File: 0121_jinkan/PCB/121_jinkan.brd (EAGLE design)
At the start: 25.4 x 33 mm, 12 parts

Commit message: 121_jinkan　ロゴ修正、リファイン
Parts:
- removed U$3: (no value), FaBo-etc:LOGO_FABO_MS_BOTTOM
- added LOGO1: (no value), component:LOGO_FABO_M
- turned R3 to 180 degrees
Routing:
- net GND: track 88.1 -> 0.00 mm, vias 14 -> 24
- net VCC: track 38.8 -> 33.4 mm
- net I/O: track 9.37 -> 11.2 mm
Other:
- board text added: "Rev.1.0.2"
- board text removed: "Rev.1.0.1"

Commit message: #121  jinkan 分圧出力回路追加
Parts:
- added R4: 9.1K, FaBo-Resistors:0603
- added SJ1: (no value), jumper:SJW
- R3: value 5.6K -> 4.7K
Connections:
- new net N$3: R4.2, SJ1.1
- net GND: now also R4.1
- net I/O: now also SJ1.2
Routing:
- net GND: track 0.00 -> 15.1 mm, vias 24 -> 23
- net I/O: track 11.2 -> 17.4 mm
- net N$3: track 0.00 -> 2.98 mm
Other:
- board text added: "Rev.1.0.3"
- board text removed: "Rev.1.0.2"
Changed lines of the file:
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@@
 <?xml version="1.0" encoding="utf-8"?>
 <!DOCTYPE eagle SYSTEM "eagle.dtd">
-<eagle version="9.6.2">
+<eagle version="9.6.0">
 <drawing>
 <settings>
-<setting alwaysvectorfont="no"/>
+<setting alwaysvectorfont="yes"/>
 <setting keepoldvectorfont="yes"/>
 <setting verticaltext="up"/>
@@
 <plain>
 <text x="3.81" y="12.065" size="1.27" layer="21" font="vector" ratio="15" rot="R90" align="bottom-center">Jinkan</text>
-<text x="5.08" y="8.89" size="1.016" layer="21" font="vector" ratio="15" rot="R90">Rev.1.0.2</text>
+<text x="5.08" y="8.89" size="1.016" layer="21" font="vector" ratio="15" rot="R90">Rev.1.0.3</text>
 <text x="22.86" y="12.065" size="0.762" layer="21" font="vector" ratio="15" rot="R90" align="top-center">Designed in Aizu</text>
 <text x="12.7" y="13.335" size="2.54" layer="21" font="vector" ratio="15" align="bottom-center">#121</text>
 <rectangle x1="13.5" y1="9.9" x2="18.7" y2="17.5" layer="22" rot="R90"/>
 <text x="7.885" y="13.45" size="2.5" layer="22" font="vector" ratio="15" rot="MR180">M</text>
+<rectangle x1="2.54" y1="13.335" x2="6.35" y2="14.605" layer="42"/>
+<rectangle x1="2.54" y1="14.605" x2="3.175" y2="15.875" layer="42"/>
+<rectangle x1="5.715" y1="14.605" x2="6.35" y2="15.875" layer="42"/>
+<rectangle x1="2.54" y1="12.065" x2="3.175" y2="13.335" layer="42"/>
+<rectangle x1="5.715" y1="12.065" x2="6.35" y2="13.335" layer="42"/>
 </plain>
 <attributes>
@@
 </element>
 <element name="U$5" library="FaBo-Transistor" package="SOT-23" value="TRANSISTOR-NPN" x="10.6" y="18.7" smashed="yes" rot="MR180"/>
-<element name="R3" library="FaBo-Resistors" package="0603" value="5.6K" x="9.7" y="15.9" smashed="yes" rot="MR180">
+<element name="R3" library="FaBo-Resistors" package="0603" value="4.7K" x="9.7" y="15.9" smashed="yes" rot="MR180">
 <attribute name="VALUE" x="9.9" y="16" size="0.8128" layer="28" font="vector" ratio="12" rot="MR180" align="center"/>
 </element>
@@
 <element name="U$7" library="FaBo-etc" package="MARK_POINT_3MM" value="" x="19.9" y="26.7" smashed="yes" rot="MR0"/>
 <element name="LOGO1" library="component" package="LOGO_FABO_M" value="" x="22.86" y="12.065" smashed="yes" rot="R90"/>
+<element name="R4" library="FaBo-Resistors" package="0603" value="9.1K" x="6.35" y="10.16" smashed="yes" rot="MR90">
+<attribute name="VALUE" x="6.35" y="10.16" size="0.8128" layer="28" font="vector" ratio="12" rot="MR90" align="center"/>
+</element>
+<element name="SJ1" library="jumper" library_urn="urn:adsk.eagle:library:252" package="SJW" package3d_urn="urn:adsk.eagle:package:15507/1" value="" x="4.445" y="13.97" smashed="yes" rot="MR90">
+<attribute name="NAME" x="6.223" y="11.811" size="1.27" layer="26" font="vector" ratio="15" rot="MR90"/>
+<attribute name="POPULARITY" value="3" x="0.635" y="14.605" size="1.778" layer="28" rot="MR90" display="off"/>
+<attribute name="VALUE" x="4.445" y="14.97" size="0.02" layer="28" rot="MR90"/>
+</element>
 </elements>
 <signals>
@@
 <via x="10.16" y="14.351" extent="1-16" drill="0.3048"/>
 <via x="13.97" y="12.319" extent="1-16" drill="0.3048"/>
-<via x="7.493" y="12.192" extent="1-16" drill="0.3048"/>
+<via x="8.128" y="9.017" extent="1-16" drill="0.3048"/>
 <via x="7.112" y="15.494" extent="1-16" drill="0.3048"/>
 <via x="7.366" y="18.415" extent="1-16" drill="0.3048"/>
@@
 <via x="8.128" y="24.384" extent="1-16" drill="0.3048"/>
 <via x="6.858" y="21.971" extent="1-16" drill="0.3048"/>
-<via x="7.493" y="10.287" extent="1-16" drill="0.3048"/>
-<via x="7.493" y="8.382" extent="1-16" drill="0.3048"/>
+<via x="7.493" y="7.747" extent="1-16" drill="0.3048"/>
+<contactref element="R4" pad="1"/>
+<wire x1="6.35" y1="6.35" x2="8.255" y2="4.445" width="0.4064" layer="16"/>
+<wire x1="14.7" y1="5.81" x2="14.7" y2="8.255" width="0.4064" layer="16"/>
+<wire x1="6.35" y1="9.31" x2="6.35" y2="6.35" width="0.4064" layer="16"/>
+<wire x1="8.255" y1="4.445" x2="13.335" y2="4.445" width="0.4064" layer="16"/>
+<wire x1="13.335" y1="4.445" x2="14.7" y2="5.81" width="0.4064" layer="16"/>
 </signal>
 <signal name="I/O">
@@
 <wire x1="9.88" y1="17.5" x2="10.6" y2="17.5" width="0.4064" layer="16"/>
 <wire x1="8.85" y1="15.9" x2="8.85" y2="16.47" width="0.4064" layer="16"/>
-<wire x1="8.85" y1="16.47" x2="9.88" y2="17.5" width="0.4064" layer="16"/>
+<wire x1="8.85" y1="16.47" x2="9.525" y2="17.145" width="0.4064" layer="16"/>
+<wire x1="9.525" y1="17.145" x2="9.88" y2="17.5" width="0.4064" layer="16"/>
 <wire x1="10.7" y1="10.89" x2="10.7" y2="8.255" width="0.4064" layer="16"/>
 <wire x1="8.85" y1="15.9" x2="8.85" y2="12.74" width="0.4064" layer="16"/>
 <wire x1="8.85" y1="12.74" x2="10.7" y2="10.89" width="0.4064" layer="16"/>
+<contactref element="SJ1" pad="2"/>
+<wire x1="4.445" y1="15.24" x2="4.445" y2="15.875" width="0.4064" layer="16"/>
+<wire x1="4.445" y1="15.875" x2="5.715" y2="17.145" width="0.4064" layer="16"/>
+<wire x1="5.715" y1="17.145" x2="9.525" y2="17.145" width="0.4064" layer="16"/>
 </signal>
 <signal name="VCC">
@@
 <wire x1="9.65" y1="20.4" x2="9.65" y2="19.9" width="0.4064" layer="16"/>
 </signal>
+<signal name="N$3">
+<contactref element="R4" pad="2"/>
+<contactref element="SJ1" pad="1"/>
+<wire x1="4.445" y1="12.7" x2="5.08" y2="12.065" width="0.4064" layer="16"/>
+<wire x1="5.08" y1="12.065" x2="5.08" y2="11.43" width="0.4064" layer="16"/>
+<wire x1="5.08" y1="11.43" x2="5.5" y2="11.01" width="0.4064" layer="16"/>
+<wire x1="5.5" y1="11.01" x2="6.35" y2="11.01" width="0.4064" layer="16"/>
+</signal>
 </signals>
 <mfgpreviewcolors>
@@
 </board>
 </drawing>
+<compatibility>
+<note version="8.2" severity="warning">
+Since Version 8.2, EAGLE supports online libraries. The ids
+of those online libraries will not be understood (or retained)
+with this version.
+</note>
+<note version="8.3" severity="warning">
+Since Version 8.3, EAGLE supports URNs for individual library
+assets (packages, symbols, and devices). The URNs of those assets
+will not be understood (or retained) with this version.
+</note>
+<note version="8.3" severity="warning">
+Since Version 8.3, EAGLE supports the association of 3D packages
+with devices in libraries, schematics, and board files. Those 3D
+packages will not be understood (or retained) with this version.
+</note>
+</compatibility>
 </eagle>

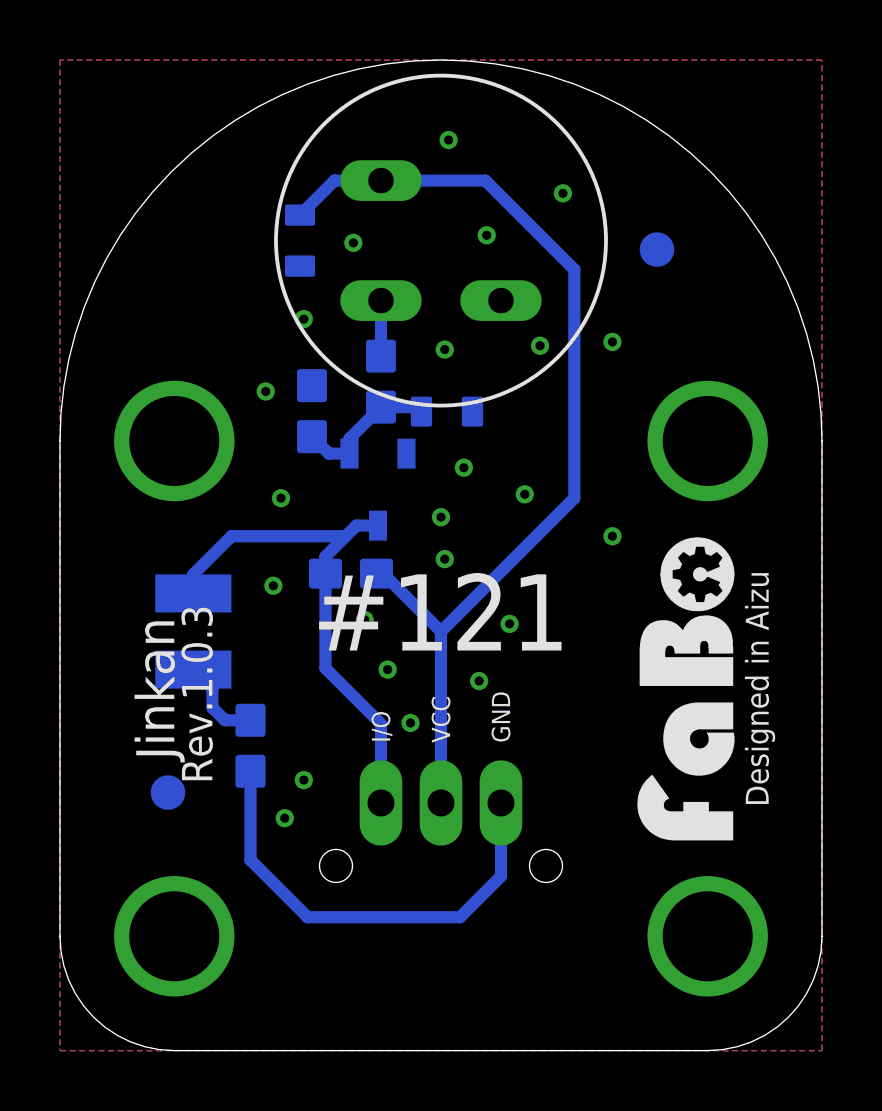
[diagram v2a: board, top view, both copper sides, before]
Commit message: #0121 Jinkan アップデート　ラズパイ、JetsonNano対応
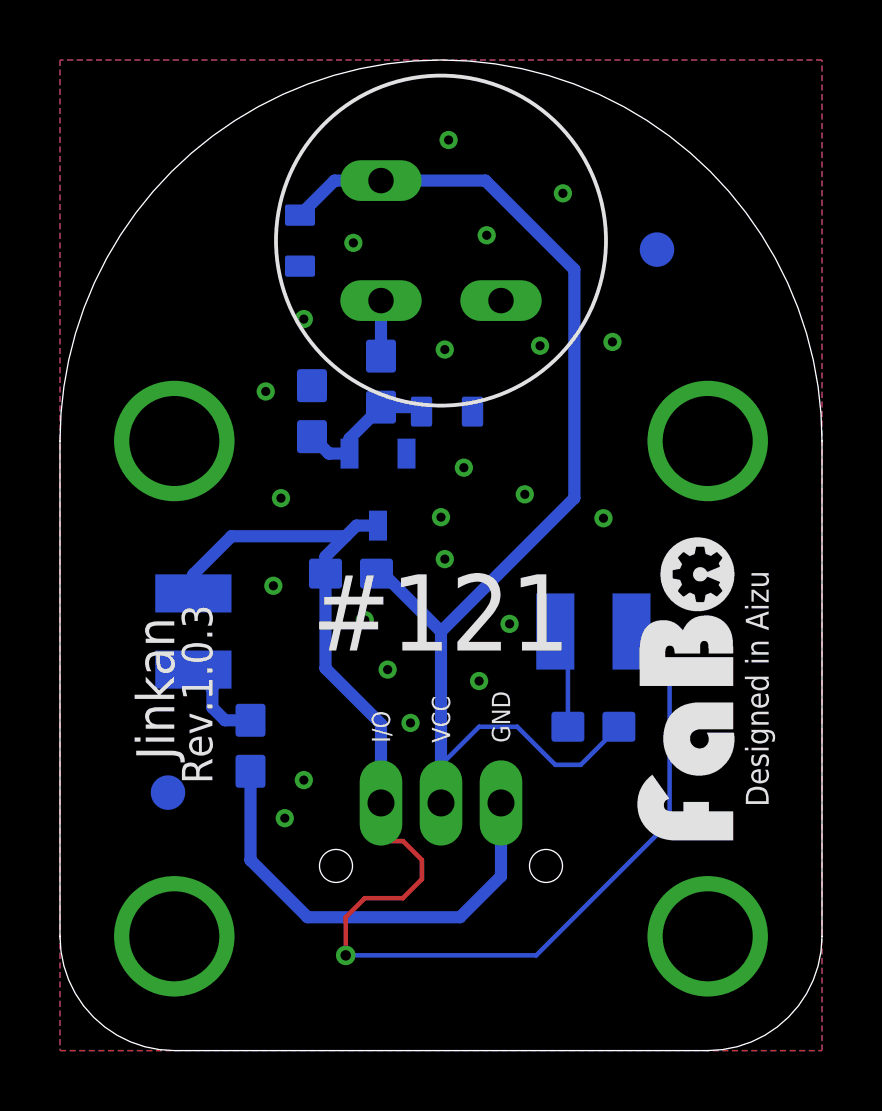
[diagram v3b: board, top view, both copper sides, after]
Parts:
- added R5: 1.2K, FaBo-Resistors:0603
- added SJ2: (no value), jumper:SJW
- C2: value (none) -> 0.1uF
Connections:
- new net N$4: R5.1, SJ2.2
- net I/O: now also SJ2.1
- net VCC: now also R5.2
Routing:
- net I/O: track 17.4 -> 44.7 mm, vias 0 -> 1
- net VCC: track 33.4 -> 42.2 mm
- net N$4: track 0.00 -> 3.35 mm
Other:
- board text added: "SJ2"
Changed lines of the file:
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@@
 <drawing>
 <settings>
-<setting alwaysvectorfont="yes"/>
+<setting alwaysvectorfont="no"/>
 <setting keepoldvectorfont="yes"/>
 <setting verticaltext="up"/>
 </settings>
-<grid distance="25" unitdist="mil" unit="mil" style="lines" multiple="1" display="yes" altdistance="5" altunitdist="mil" altunit="mil"/>
+<grid distance="0.1" unitdist="mm" unit="mm" style="lines" multiple="1" display="yes" altdistance="0.1" altunitdist="mm" altunit="mm"/>
 <layers>
 <layer number="1" name="Top" color="4" fill="1" visible="yes" active="yes"/>
@@
 <text x="22.86" y="12.065" size="0.762" layer="21" font="vector" ratio="15" rot="R90" align="top-center">Designed in Aizu</text>
 <text x="12.7" y="13.335" size="2.54" layer="21" font="vector" ratio="15" align="bottom-center">#121</text>
-<rectangle x1="13.5" y1="9.9" x2="18.7" y2="17.5" layer="22" rot="R90"/>
-<text x="7.885" y="13.45" size="2.5" layer="22" font="vector" ratio="15" rot="MR180">M</text>
+<text x="6.53" y="14.05" size="2.5" layer="22" font="vector" ratio="15" rot="MR180">M</text>
 <rectangle x1="2.54" y1="13.335" x2="6.35" y2="14.605" layer="42"/>
 <rectangle x1="2.54" y1="14.605" x2="3.175" y2="15.875" layer="42"/>
@@
 <rectangle x1="2.54" y1="12.065" x2="3.175" y2="13.335" layer="42"/>
 <rectangle x1="5.715" y1="12.065" x2="6.35" y2="13.335" layer="42"/>
+<rectangle x1="9.1" y1="10.6" x2="15.1" y2="14.6" layer="22"/>
+<text x="19.4" y="15.9" size="1.27" layer="22" font="vector" ratio="15" rot="MR0">SJ2</text>
+<rectangle x1="17.2" y1="12.2" x2="18.3" y2="15.7" layer="42"/>
+<rectangle x1="15.5" y1="15.3" x2="17.2" y2="15.6" layer="42"/>
+<rectangle x1="18.3" y1="15.3" x2="19.9" y2="15.6" layer="42"/>
+<rectangle x1="15.8" y1="12.4" x2="16.8" y2="12.6" layer="42"/>
+<rectangle x1="18.5" y1="12.3" x2="19.5" y2="12.6" layer="42"/>
 </plain>
 <attributes>
@@
 <attribute name="VALUE" x="10.5" y="22.5" size="0.8128" layer="28" font="vector" ratio="12" rot="MR90" align="center"/>
 </element>
-<element name="C2" library="FaBo-Capacitor" package="0603-NARROW" value="" x="12.9" y="21.3" smashed="yes" rot="MR0">
+<element name="C2" library="FaBo-Capacitor" package="0603-NARROW" value="0.1uF" x="12.9" y="21.3" smashed="yes" rot="MR0">
 <attribute name="VALUE" x="12.9" y="21.3" size="0.8128" layer="28" font="vector" ratio="12" rot="MR0" align="center"/>
 </element>
@@
 </element>
 <element name="SJ1" library="jumper" library_urn="urn:adsk.eagle:library:252" package="SJW" package3d_urn="urn:adsk.eagle:package:15507/1" value="" x="4.445" y="13.97" smashed="yes" rot="MR90">
-<attribute name="NAME" x="6.223" y="11.811" size="1.27" layer="26" font="vector" ratio="15" rot="MR90"/>
+<attribute name="NAME" x="5.923" y="16.411" size="1.27" layer="26" font="vector" ratio="15" rot="MR0"/>
 <attribute name="POPULARITY" value="3" x="0.635" y="14.605" size="1.778" layer="28" rot="MR90" display="off"/>
 <attribute name="VALUE" x="4.445" y="14.97" size="0.02" layer="28" rot="MR90"/>
+</element>
+<element name="R5" library="FaBo-Resistors" package="0603" value="1.2K" x="17.78" y="10.795" smashed="yes" rot="MR180">
+<attribute name="NAME" x="17.78" y="9.906" size="0.8128" layer="26" font="vector" ratio="12" rot="MR180" align="bottom-center"/>
+<attribute name="VALUE" x="17.78" y="10.795" size="0.8128" layer="28" font="vector" ratio="12" rot="MR180" align="center"/>
+</element>
+<element name="SJ2" library="jumper" library_urn="urn:adsk.eagle:library:252" package="SJW" package3d_urn="urn:adsk.eagle:package:15507/1" value="" x="17.78" y="13.97" smashed="yes" rot="MR0">
+<attribute name="POPULARITY" value="3" x="17.78" y="13.97" size="1.778" layer="28" rot="MR0" display="off"/>
+<attribute name="VALUE" x="16.78" y="13.97" size="0.02" layer="28" rot="MR0"/>
 </element>
 </elements>
@@
 <contactref element="C2" pad="1"/>
 <contactref element="U$5" pad="2"/>
-<via x="18.415" y="17.145" extent="1-16" drill="0.3048"/>
+<via x="18.115" y="17.745" extent="1-16" drill="0.3048"/>
 <via x="11.684" y="10.922" extent="1-16" drill="0.3048"/>
 <via x="10.922" y="12.7" extent="1-16" drill="0.3048"/>
@@
 <wire x1="4.445" y1="15.875" x2="5.715" y2="17.145" width="0.4064" layer="16"/>
 <wire x1="5.715" y1="17.145" x2="9.525" y2="17.145" width="0.4064" layer="16"/>
+<contactref element="SJ2" pad="1"/>
+<wire x1="19.05" y1="13.97" x2="20.32" y2="12.7" width="0.1524" layer="16"/>
+<wire x1="15.875" y1="3.175" x2="9.525" y2="3.175" width="0.1524" layer="16"/>
+<via x="9.525" y="3.175" extent="1-16" drill="0.35"/>
+<wire x1="9.525" y1="3.175" x2="9.525" y2="4.445" width="0.1524" layer="1"/>
+<wire x1="9.525" y1="4.445" x2="10.16" y2="5.08" width="0.1524" layer="1"/>
+<wire x1="10.16" y1="5.08" x2="11.43" y2="5.08" width="0.1524" layer="1"/>
+<wire x1="11.43" y1="5.08" x2="12.065" y2="5.715" width="0.1524" layer="1"/>
+<wire x1="12.065" y1="5.715" x2="12.065" y2="6.35" width="0.1524" layer="1"/>
+<wire x1="12.065" y1="6.35" x2="11.43" y2="6.985" width="0.1524" layer="1"/>
+<wire x1="11.43" y1="6.985" x2="10.795" y2="6.985" width="0.1524" layer="1"/>
+<wire x1="10.795" y1="6.985" x2="10.7" y2="7.08" width="0.1524" layer="1"/>
+<wire x1="10.7" y1="7.08" x2="10.7" y2="8.255" width="0.1524" layer="1"/>
+<wire x1="20.32" y1="12.7" x2="20.32" y2="7.62" width="0.1524" layer="16"/>
+<wire x1="20.32" y1="7.62" x2="15.875" y2="3.175" width="0.1524" layer="16"/>
 </signal>
 <signal name="VCC">
@@
 <contactref element="U$4" pad="VDD"/>
 <contactref element="C1" pad="2"/>
-<contactref element="R3" pad="2"/>
 <wire x1="17.145" y1="18.415" x2="17.145" y2="26.035" width="0.4064" layer="16"/>
 <wire x1="10.7" y1="29" x2="14.18" y2="29" width="0.4064" layer="16"/>
@@
 <wire x1="12.7" y1="8.255" x2="12.7" y2="13.97" width="0.4064" layer="16"/>
 <wire x1="12.7" y1="13.97" x2="17.145" y2="18.415" width="0.4064" layer="16"/>
+<contactref element="R5" pad="2"/>
+<contactref element="R3" pad="2"/>
+<wire x1="18.63" y1="10.795" x2="17.36" y2="9.525" width="0.1524" layer="16"/>
+<wire x1="17.36" y1="9.525" x2="16.51" y2="9.525" width="0.1524" layer="16"/>
+<wire x1="16.51" y1="9.525" x2="15.24" y2="10.795" width="0.1524" layer="16"/>
+<wire x1="15.24" y1="10.795" x2="13.97" y2="10.795" width="0.1524" layer="16"/>
+<wire x1="12.7" y1="9.525" x2="12.7" y2="8.255" width="0.1524" layer="16"/>
+<wire x1="13.97" y1="10.795" x2="12.7" y2="9.525" width="0.1524" layer="16"/>
 <wire x1="10.55" y1="15.9" x2="10.77" y2="15.9" width="0.4064" layer="16"/>
 <wire x1="10.77" y1="15.9" x2="12.7" y2="13.97" width="0.4064" layer="16"/>
@@
 <wire x1="5.5" y1="11.01" x2="6.35" y2="11.01" width="0.4064" layer="16"/>
 </signal>
+<signal name="N$4">
+<contactref element="SJ2" pad="2"/>
+<contactref element="R5" pad="1"/>
+<wire x1="16.51" y1="13.97" x2="16.93" y2="13.55" width="0.1524" layer="16"/>
+<wire x1="16.93" y1="13.55" x2="16.93" y2="10.795" width="0.1524" layer="16"/>
+</signal>
 </signals>
